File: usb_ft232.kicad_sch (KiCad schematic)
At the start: 16 parts, among them P1 10164359-00011LF, U3 FT232RL, U6 USBLC6-2SC6

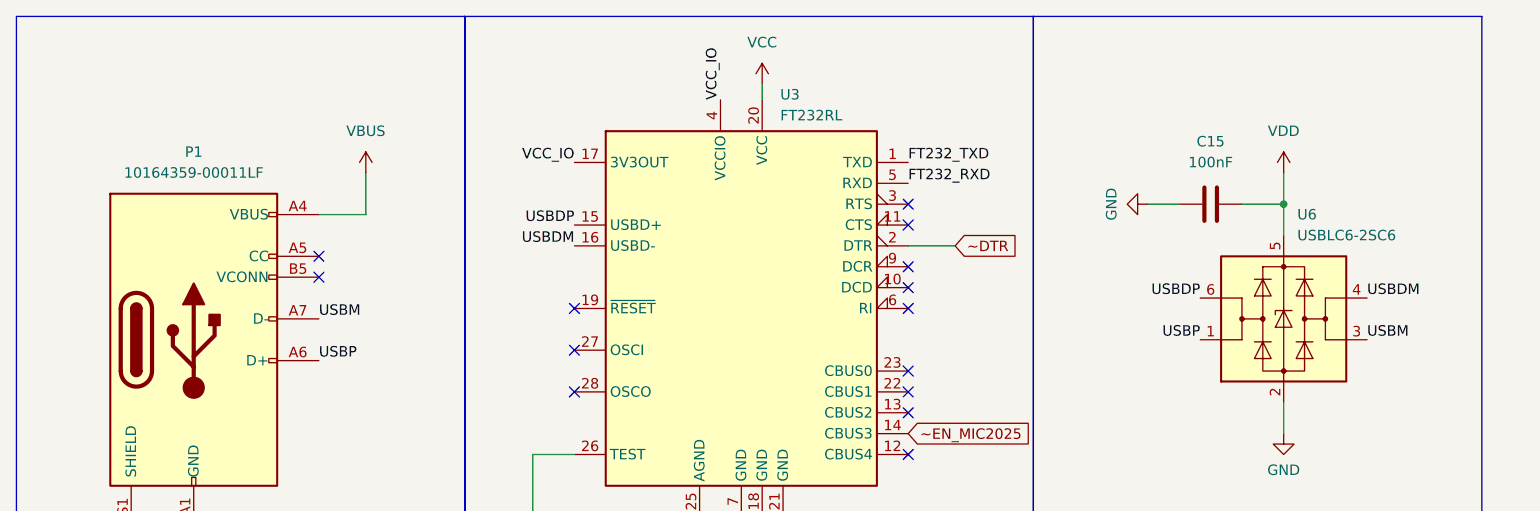
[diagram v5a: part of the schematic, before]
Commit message: [WIP] pcb design with minor fixes in schema to have cleanest routing
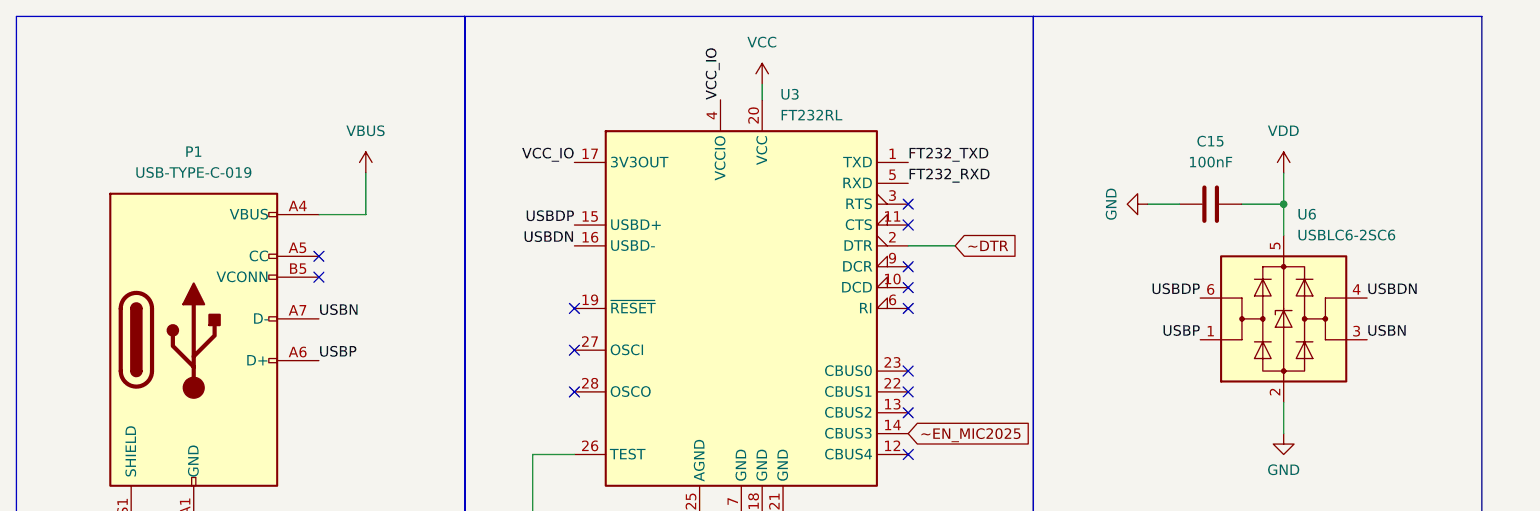
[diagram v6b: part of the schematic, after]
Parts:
- C10, C6: footprint (none) -> Capacitor_SMD:CP_Elec_4x5.4; Fab: (none) -> ROQANG; Man #: (none) -> CK1H4R7M-CRC54
- C15, C19, C7, C9: footprint (none) -> Capacitor_SMD:C_1206_3216Metric; Fab: (none) -> Yageo; Man #: (none) -> CC1206KKX7RCBB103
- C8: footprint (none) -> Capacitor_SMD:C_1206_3216Metric
- F1: footprint (none) -> Fuse:Fuse_1210_3225Metric; Fab: (none) -> Jinrui Electronic Materials Co.; Man #: (none) -> JK-SMD1210-010/30V
- L1: footprint (none) -> Resistor_SMD:R_1206_3216Metric; Man #: (none) -> GZ3216D000TF
- P1: value 10164359-00011LF -> USB-TYPE-C-019; footprint Connector_USB:USB_C_Receptacle_GCT_USB4125-xx-x_6P_TopMnt_Horizontal -> Connector_USB:USB_C_Receptacle_GCT_USB4105-xx-A_16P_TopMnt_Horizontal; Fab: (none) -> dealon; Man #: (none) -> USB-TYPE-C-019
- R14: footprint (none) -> Resistor_SMD:R_1206_3216Metric; Fab: (none) -> VO; Man #: (none) -> SCR1206J1M
- R5: footprint (none) -> Resistor_SMD:R_1206_3216Metric; Fab: (none) -> VO; Man #: (none) -> SCR1206J10K
- R7, R8: footprint (none) -> Resistor_SMD:R_1206_3216Metric; Fab: (none) -> RALEC; Man #: (none) -> RTT06000JTP
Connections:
- net USBDM renamed USBDN
- net USBM renamed USBN
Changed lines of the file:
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@@
     (effects (font (size 1.27 1.27)) (justify right bottom))
   )
-  (label "USBDM" (at 183.515 52.705 0) (fields_autoplaced)
+  (label "USBDN" (at 183.515 52.705 0) (fields_autoplaced)
     (effects (font (size 1.27 1.27)) (justify left bottom))
   )
@@
     (effects (font (size 1.27 1.27)) (justify left bottom))
   )
-  (label "USBDM" (at 86.995 46.355 180) (fields_autoplaced)
+  (label "USBDN" (at 86.995 46.355 180) (fields_autoplaced)
     (effects (font (size 1.27 1.27)) (justify right bottom))
   )
@@
     (effects (font (size 1.27 1.27)) (justify right bottom))
   )
-  (label "USBM" (at 183.515 57.785 0) (fields_autoplaced)
+  (label "USBN" (at 183.515 57.785 0) (fields_autoplaced)
     (effects (font (size 1.27 1.27)) (justify left bottom))
   )
-  (label "USBM" (at 55.88 55.245 0) (fields_autoplaced)
+  (label "USBN" (at 55.88 55.245 0) (fields_autoplaced)
     (effects (font (size 1.27 1.27)) (justify left bottom))
   )
@@
       (effects (font (size 1.27 1.27)))
     )
-    (property "Footprint" "" (at 189.23 124.333 90)
+    (property "Footprint" "Resistor_SMD:R_1206_3216Metric" (at 189.23 124.333 90)
       (effects (font (size 1.27 1.27)) hide)
     )
@@
       (effects (font (size 1.27 1.27)) hide)
     )
+    (property "Man #:" "SCR1206J1M" (at 189.23 122.555 0)
+      (effects (font (size 1.27 1.27)) hide)
+    )
+    (property "Fab:" "VO" (at 189.23 122.555 0)
+      (effects (font (size 1.27 1.27)) hide)
+    )
     (pin "1")
     (pin "2")
@@
       (effects (font (size 1.27 1.27)) (justify left))
     )
-    (property "Footprint" "" (at 193.9798 131.445 0)
+    (property "Footprint" "Capacitor_SMD:C_1206_3216Metric" (at 193.9798 131.445 0)
       (effects (font (size 1.27 1.27)) hide)
     )
@@
       (effects (font (size 1.27 1.27)) hide)
     )
+    (property "Man #:" "CC1206KKX7RCBB103" (at 194.945 127.635 0)
+      (effects (font (size 1.27 1.27)) hide)
+    )
+    (property "Fab:" "Yageo" (at 194.945 127.635 0)
+      (effects (font (size 1.27 1.27)) hide)
+    )
     (pin "1")
     (pin "2")
@@
       (effects (font (size 1.27 1.27)) (justify left))
     )
-    (property "Footprint" "" (at 39.6748 143.51 0)
+    (property "Footprint" "Capacitor_SMD:C_1206_3216Metric" (at 39.6748 143.51 0)
       (effects (font (size 1.27 1.27)) hide)
     )
@@
       (effects (font (size 1.27 1.27)) hide)
     )
+    (property "Man #:" "" (at 40.64 139.7 0)
+      (effects (font (size 1.27 1.27)) hide)
+    )
     (pin "1")
     (pin "2")
@@
       (effects (font (size 1.27 1.27)))
     )
-    (property "Footprint" "" (at 34.29 132.588 90)
+    (property "Footprint" "Fuse:Fuse_1210_3225Metric" (at 34.29 132.588 90)
       (effects (font (size 1.27 1.27)) hide)
     )
@@
       (effects (font (size 1.27 1.27)) hide)
     )
+    (property "Man #:" "JK-SMD1210-010/30V" (at 34.29 130.81 0)
+      (effects (font (size 1.27 1.27)) hide)
+    )
+    (property "Fab:" "Jinrui Electronic Materials Co." (at 34.29 130.81 0)
+      (effects (font (size 1.27 1.27)) hide)
+    )
     (pin "1")
     (pin "2")
@@
       (effects (font (size 1.27 1.27)))
     )
-    (property "Footprint" "" (at 160.02 140.208 90)
+    (property "Footprint" "Resistor_SMD:R_1206_3216Metric" (at 160.02 140.208 90)
       (effects (font (size 1.27 1.27)) hide)
     )
@@
       (effects (font (size 1.27 1.27)) hide)
     )
+    (property "Man #:" "RTT06000JTP" (at 160.02 138.43 0)
+      (effects (font (size 1.27 1.27)) hide)
+    )
+    (property "Fab:" "RALEC" (at 160.02 138.43 0)
+      (effects (font (size 1.27 1.27)) hide)
+    )
     (pin "1")
     (pin "2")
@@
     )
     (property "Datasheet" "https://www.ftdichip.com/Support/Documents/DataSheets/ICs/DS_FT232R.pdf" (at 107.315 53.975 0)
+      (effects (font (size 1.27 1.27)) hide)
+    )
+    (property "Man #:" "" (at 107.315 53.975 0)
       (effects (font (size 1.27 1.27)) hide)
     )
@@
       (effects (font (size 1.27 1.27)) hide)
     )
+    (property "Man #:" "" (at 173.355 55.245 0)
+      (effects (font (size 1.27 1.27)) hide)
+    )
     (pin "1")
     (pin "2")
@@
       (effects (font (size 1.27 1.27)))
     )
-    (property "Value" "10164359-00011LF" (at 40.64 37.465 0)
-      (effects (font (size 1.27 1.27)))
-    )
-    (property "Footprint" "Connector_USB:USB_C_Receptacle_GCT_USB4125-xx-x_6P_TopMnt_Horizontal" (at 44.45 57.785 0)
-      (effects (font (size 1.27 1.27)) hide)
-    )
-    (property "Datasheet" "https://www.usb.org/sites/default/files/documents/usb_type-c.zip" (at 44.45 57.785 0)
+    (property "Value" "USB-TYPE-C-019" (at 40.64 37.465 0)
+      (effects (font (size 1.27 1.27)))
+    )
+    (property "Footprint" "Connector_USB:USB_C_Receptacle_GCT_USB4105-xx-A_16P_TopMnt_Horizontal" (at 44.45 57.785 0)
+      (effects (font (size 1.27 1.27)) hide)
+    )
+    (property "Datasheet" "https://datasheet.lcsc.com/lcsc/2201121330_DEALON-USB-TYPE-C-019_C2927039.pdf" (at 44.45 57.785 0)
       (effects (font (size 1.27 1.27)) hide)
     )
@@
     )
     (property "Datasheet:" "https://cdn.amphenol-cs.com/media/wysiwyg/files/drawing/10164359.pdf" (at 40.64 57.785 0)
+      (effects (font (size 1.27 1.27)) hide)
+    )
+    (property "Man #:" "USB-TYPE-C-019" (at 40.64 57.785 0)
+      (effects (font (size 1.27 1.27)) hide)
+    )
+    (property "Fab:" "dealon" (at 40.64 57.785 0)
       (effects (font (size 1.27 1.27)) hide)
     )
@@
       (effects (font (size 1.27 1.27)) (justify left))
     )
-    (property "Footprint" "" (at 101.9048 139.7 0)
+    (property "Footprint" "Capacitor_SMD:C_1206_3216Metric" (at 101.9048 139.7 0)
       (effects (font (size 1.27 1.27)) hide)
     )
@@
       (effects (font (size 1.27 1.27)) hide)
     )
+    (property "Man #:" "CC1206KKX7RCBB103" (at 102.87 135.89 0)
+      (effects (font (size 1.27 1.27)) hide)
+    )
+    (property "Fab:" "Yageo" (at 102.87 135.89 0)
+      (effects (font (size 1.27 1.27)) hide)
+    )
     (pin "1")
     (pin "2")
@@
       (effects (font (size 1.27 1.27)))
     )
-    (property "Footprint" "" (at 109.22 130.048 90)
+    (property "Footprint" "Resistor_SMD:R_1206_3216Metric" (at 109.22 130.048 90)
       (effects (font (size 1.27 1.27)) hide)
     )
@@
       (effects (font (size 1.27 1.27)) hide)
     )
+    (property "Man #:" "SCR1206J10K" (at 109.22 128.27 0)
+      (effects (font (size 1.27 1.27)) hide)
+    )
+    (property "Fab:" "VO" (at 109.22 128.27 0)
+      (effects (font (size 1.27 1.27)) hide)
+    )
     (pin "1")
     (pin "2")
@@
       (effects (font (size 1.27 1.27)))
     )
-    (property "Footprint" "" (at 49.53 130.81 0)
+    (property "Footprint" "Resistor_SMD:R_1206_3216Metric" (at 49.53 130.81 0)
       (effects (font (size 1.27 1.27)) hide)
     )
@@
       (effects (font (size 1.27 1.27)) hide)
     )
+    (property "Man #:" "GZ3216D000TF" (at 49.53 130.81 0)
+      (effects (font (size 1.27 1.27)) hide)
+    )
     (pin "1")
     (pin "2")
@@
       (effects (font (size 1.27 1.27)))
     )
-    (property "Footprint" "" (at 168.275 40.3098 0)
+    (property "Footprint" "Capacitor_SMD:C_1206_3216Metric" (at 168.275 40.3098 0)
       (effects (font (size 1.27 1.27)) hide)
     )
@@
       (effects (font (size 1.27 1.27)) hide)
     )
+    (property "Man #:" "CC1206KKX7RCBB103" (at 164.465 41.275 0)
+      (effects (font (size 1.27 1.27)) hide)
+    )
+    (property "Fab:" "Yageo" (at 164.465 41.275 0)
+      (effects (font (size 1.27 1.27)) hide)
+    )
     (pin "1")
     (pin "2")
@@
       (effects (font (size 1.27 1.27)) (justify left))
     )
-    (property "Footprint" "" (at 72.6948 142.24 0)
+    (property "Footprint" "Capacitor_SMD:C_1206_3216Metric" (at 72.6948 142.24 0)
       (effects (font (size 1.27 1.27)) hide)
     )
@@
       (effects (font (size 1.27 1.27)) hide)
     )
+    (property "Man #:" "CC1206KKX7RCBB103" (at 73.66 138.43 0)
+      (effects (font (size 1.27 1.27)) hide)
+    )
+    (property "Fab:" "Yageo" (at 73.66 138.43 0)
+      (effects (font (size 1.27 1.27)) hide)
+    )
     (pin "1")
     (pin "2")
@@
       (effects (font (size 1.27 1.27)))
     )
-    (property "Footprint" "" (at 160.02 130.048 90)
+    (property "Footprint" "Resistor_SMD:R_1206_3216Metric" (at 160.02 130.048 90)
       (effects (font (size 1.27 1.27)) hide)
     )
@@
       (effects (font (size 1.27 1.27)) hide)
     )
+    (property "Man #:" "RTT06000JTP" (at 160.02 128.27 0)
+      (effects (font (size 1.27 1.27)) hide)
+    )
+    (property "Fab:" "RALEC" (at 160.02 128.27 0)
+      (effects (font (size 1.27 1.27)) hide)
+    )
     (pin "1")
     (pin "2")
@@
       (effects (font (size 1.27 1.27)) (justify left))
     )
-    (property "Footprint" "" (at 58.1152 142.24 0)
+    (property "Footprint" "Capacitor_SMD:CP_Elec_4x5.4" (at 58.1152 142.24 0)
       (effects (font (size 1.27 1.27)) hide)
     )
@@
       (effects (font (size 1.27 1.27)) hide)
     )
+    (property "Man #:" "CK1H4R7M-CRC54" (at 57.15 138.43 0)
+      (effects (font (size 1.27 1.27)) hide)
+    )
+    (property "Fab:" "	ROQANG" (at 57.15 138.43 0)
+      (effects (font (size 1.27 1.27)) hide)
+    )
     (pin "1")
     (pin "2")
@@
       (effects (font (size 1.27 1.27)) (justify left))
     )
-    (property "Footprint" "" (at 28.9052 142.24 0)
+    (property "Footprint" "Capacitor_SMD:CP_Elec_4x5.4" (at 28.9052 142.24 0)
       (effects (font (size 1.27 1.27)) hide)
     )
@@
       (effects (font (size 1.27 1.27)) hide)
     )
+    (property "Man #:" "CK1H4R7M-CRC54" (at 27.94 138.43 0)
+      (effects (font (size 1.27 1.27)) hide)
+    )
+    (property "Fab:" "	ROQANG" (at 27.94 138.43 0)
+      (effects (font (size 1.27 1.27)) hide)
+    )

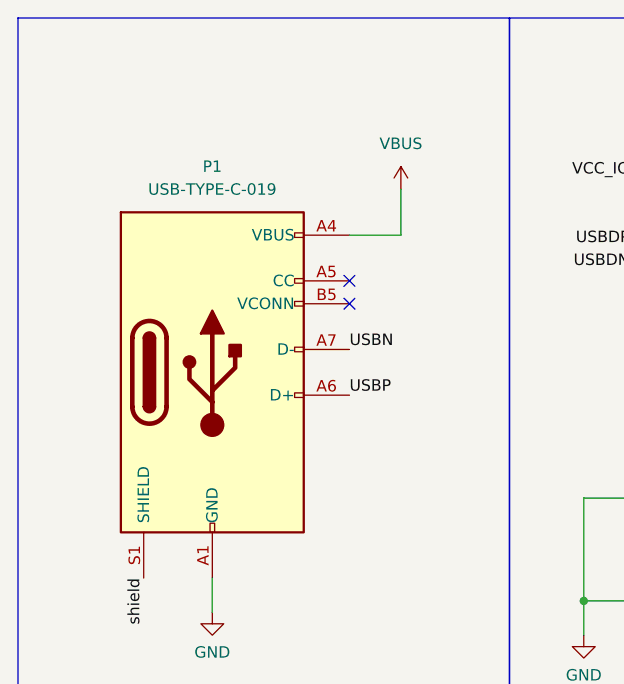
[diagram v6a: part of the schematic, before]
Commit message: text labels and route finished
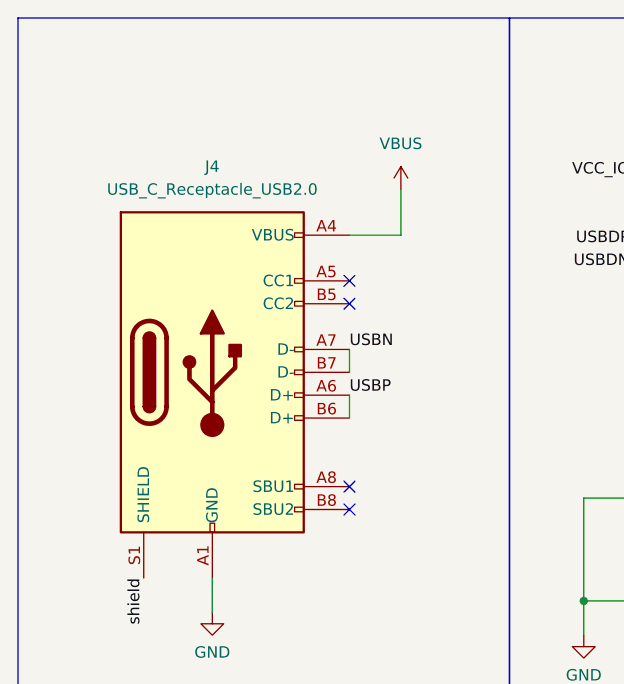
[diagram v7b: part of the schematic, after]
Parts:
- removed P1: USB-TYPE-C-019, Connector_USB:USB_C_Receptacle_GCT_USB4105-xx-A_16P_TopMnt_Horizontal, symbol Connector:USB_C_Plug_USB2.0
- added J4: USB_C_Receptacle_USB2.0, symbol Connector:USB_C_Receptacle_USB2.0
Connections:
- net GND: now also J4.A1 (GND), J4.A12 (GND), J4.B1 (GND), J4.B12 (GND)
- net USBN: now also J4.A7 (D-), J4.B7 (D-)
- net USBP: now also J4.A6 (D+), J4.B6 (D+)
- net VBUS: now also J4.A4 (VBUS), J4.A9 (VBUS), J4.B4 (VBUS), J4.B9 (VBUS)
- net shield: now also J4.S1 (SHIELD)
- no-connect marks 14 -> 16
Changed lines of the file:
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@@
   (no_connect (at 86.995 59.055))
   (no_connect (at 86.995 53.975))
+  (no_connect (at 55.88 70.485))
   (no_connect (at 127.635 51.435))
   (no_connect (at 127.635 71.755))
@@
   (no_connect (at 86.995 64.135))
   (no_connect (at 127.635 66.675))
+  (no_connect (at 55.88 73.025))
   (no_connect (at 127.635 43.815))
   (wire (pts (xy 61.595 37.465) (xy 61.595 42.545))
@@
     (stroke (width 0) (type default))
   )
+  (wire (pts (xy 55.88 55.245) (xy 55.88 57.785))
+    (stroke (width 0) (type default))
+  )
   (wire (pts (xy 86.995 71.755) (xy 81.915 71.755))
     (stroke (width 0) (type default))
@@
   )
   (wire (pts (xy 40.64 143.51) (xy 40.64 147.32))
+    (stroke (width 0) (type default))
+  )
+  (wire (pts (xy 55.88 60.325) (xy 55.88 62.865))
     (stroke (width 0) (type default))
   )
@@
     )
   )
-  (symbol (lib_id "Connector:USB_C_Plug_USB2.0") (at 40.64 57.785 0) (unit 1)
-    (in_bom yes) (on_board yes) (dnp no) (fields_autoplaced)
-    (property "Reference" "P1" (at 40.64 34.925 0)
-      (effects (font (size 1.27 1.27)))
-    )
-    (property "Value" "USB-TYPE-C-019" (at 40.64 37.465 0)
-      (effects (font (size 1.27 1.27)))
-    )
-    (property "Footprint" "Connector_USB:USB_C_Receptacle_GCT_USB4105-xx-A_16P_TopMnt_Horizontal" (at 44.45 57.785 0)
-      (effects (font (size 1.27 1.27)) hide)
-    )
-    (property "Datasheet" "https://datasheet.lcsc.com/lcsc/2201121330_DEALON-USB-TYPE-C-019_C2927039.pdf" (at 44.45 57.785 0)
-      (effects (font (size 1.27 1.27)) hide)
-    )
-    (property "Fabr.: " "Amphenol FCI" (at 40.64 57.785 0)
-      (effects (font (size 1.27 1.27)) hide)
-    )
-    (property "Datasheet:" "https://cdn.amphenol-cs.com/media/wysiwyg/files/drawing/10164359.pdf" (at 40.64 57.785 0)
-      (effects (font (size 1.27 1.27)) hide)
-    )
-    (property "Man #:" "USB-TYPE-C-019" (at 40.64 57.785 0)
-      (effects (font (size 1.27 1.27)) hide)
-    )
-    (property "Fab:" "dealon" (at 40.64 57.785 0)
-      (effects (font (size 1.27 1.27)) hide)
-    )
-    (pin "A1")
-    (pin "A12")
-    (pin "A4")
-    (pin "A5")
-    (pin "A6")
-    (pin "A7")
-    (pin "A9")
-    (pin "B1")
-    (pin "B12")
-    (pin "B4")
-    (pin "B5")
-    (pin "B9")
-    (pin "S1")
-    (instances
-      (project "JTAGFinder"
-        (path "/204d557f-3c83-43db-b1fd-628e15efe3d8/651e631a-de0f-4a69-a119-5cdead14cfb1"
-          (reference "P1") (unit 1)
-        )
-        (path "/204d557f-3c83-43db-b1fd-628e15efe3d8/1bc3728f-429c-4b4e-ad94-277c4090b0e7"
-          (reference "P2") (unit 1)
-        )
-      )
-    )
-  )
   (symbol (lib_id "power:GND") (at 102.87 143.51 0) (unit 1)
     (in_bom yes) (on_board yes) (dnp no) (fields_autoplaced)
@@
         )
       )
+    )
+  )
+  (symbol (lib_id "Connector:USB_C_Receptacle_USB2.0") (at 40.64 57.785 0) (unit 1)
+    (in_bom yes) (on_board yes) (dnp no) (fields_autoplaced)
+    (property "Reference" "J4" (at 40.64 34.925 0)
+      (effects (font (size 1.27 1.27)))
+    )
+    (property "Value" "USB_C_Receptacle_USB2.0" (at 40.64 37.465 0)
+      (effects (font (size 1.27 1.27)))
+    )
+    (property "Footprint" "" (at 44.45 57.785 0)
+      (effects (font (size 1.27 1.27)) hide)
+    )
+    (property "Datasheet" "https://www.usb.org/sites/default/files/documents/usb_type-c.zip" (at 44.45 57.785 0)
+      (effects (font (size 1.27 1.27)) hide)
+    )
+    (pin "B7")
+    (pin "B5")
+    (pin "A12")
+    (pin "A4")
+    (pin "B4")
+    (pin "A5")
+    (pin "B12")
+    (pin "A1")
+    (pin "A8")
+    (pin "A6")
+    (pin "A7")
+    (pin "A9")
+    (pin "B8")
+    (pin "S1")
+    (pin "B1")
+    (pin "B6")
+    (pin "B9")
+    (instances
+      (project "JTAGFinder"
+        (path "/204d557f-3c83-43db-b1fd-628e15efe3d8/1bc3728f-429c-4b4e-ad94-277c4090b0e7"
+          (reference "J4") (unit 1)
+        )
+      )

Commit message: finished rev1
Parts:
- J4: footprint (none) -> Connector_USB:USB_C_Receptacle_HRO_TYPE-C-31-M-12
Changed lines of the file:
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@@
       (effects (font (size 1.27 1.27)))
     )
-    (property "Footprint" "" (at 44.45 57.785 0)
+    (property "Footprint" "Connector_USB:USB_C_Receptacle_HRO_TYPE-C-31-M-12" (at 44.45 57.785 0)
       (effects (font (size 1.27 1.27)) hide)
     )
